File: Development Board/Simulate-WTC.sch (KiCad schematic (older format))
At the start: 5 parts

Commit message: main sheets created
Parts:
- J? (x2): symbol conn:GS3 -> QPACE-DevelopmentBoard-rescue:GS3-conn
- R? (x2): symbol device:R -> QPACE-DevelopmentBoard-rescue:R-device
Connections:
- net labels added: CCDR_UART_RX, CCDR_UART_TX, I2C_SCK, NRST, RF_UART_RX, RF_UART_TX, SWCLK, SWDIO, SWO
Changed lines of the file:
@@
 EESchema Schematic File Version 4
 LIBS:QPACE-DevelopmentBoard-cache
-LIBS:WTC-cache
 EELAYER 26 0
 EELAYER END
 $Descr A4 11693 8268
 encoding utf-8
-Sheet 3 3
+Sheet 3 9
 Title ""
 Date ""
@@
 BOOT0
 $Comp
-L device:R R?
+L QPACE-DevelopmentBoard-rescue:R-device R?
 U 1 1 5C997057
 P 1700 2800
+AR Path="/5C997057" Ref="R?"  Part="1"
+AR Path="/5C7F8729/5C997057" Ref="R?"  Part="1"
 F 0 "R?" V 1907 2800 50  0000 C CNN
 F 1 "100k" V 1816 2800 50  0000 C CNN
@@
 $EndComp
 $Comp
-L conn:GS3 J?
+L QPACE-DevelopmentBoard-rescue:GS3-conn J?
 U 1 1 5C9970FC
 P 1400 2800
+AR Path="/5C9970FC" Ref="J?"  Part="1"
+AR Path="/5C7F8729/5C9970FC" Ref="J?"  Part="1"
 F 0 "J?" H 1400 3105 50  0000 C CNN
 F 1 "GS3" H 1400 3014 50  0000 C CNN
@@
 $EndComp
 $Comp
-L device:R R?
+L QPACE-DevelopmentBoard-rescue:R-device R?
 U 1 1 5C9971B9
 P 1700 3300
+AR Path="/5C9971B9" Ref="R?"  Part="1"
+AR Path="/5C7F8729/5C9971B9" Ref="R?"  Part="1"
 F 0 "R?" V 1907 3300 50  0000 C CNN
 F 1 "100k" V 1816 3300 50  0000 C CNN
@@
 $EndComp
 $Comp
-L conn:GS3 J?
+L QPACE-DevelopmentBoard-rescue:GS3-conn J?
 U 1 1 5C9971DB
 P 1400 3300
+AR Path="/5C9971DB" Ref="J?"  Part="1"
+AR Path="/5C7F8729/5C9971DB" Ref="J?"  Part="1"
 F 0 "J?" H 1400 3605 50  0000 C CNN
 F 1 "GS3" H 1400 3514 50  0000 C CNN
@@
 NoConn ~ 3100 4500
 NoConn ~ 3100 4400
+Text HLabel 9000 1700 2    50   Input ~ 0
+SWCLK
+Text HLabel 9000 1800 2    50   Input ~ 0
+SWDIO
+Text HLabel 9000 1900 2    50   Input ~ 0
+NRST
+Text HLabel 9000 2000 2    50   Input ~ 0
+SWO
+Text HLabel 9000 2150 2    50   Input ~ 0
+RF_UART_TX
+Text HLabel 9000 2250 2    50   Input ~ 0
+RF_UART_RX
+Text HLabel 9000 2350 2    50   Input ~ 0
+CCDR_UART_RX
+Text HLabel 9000 2450 2    50   Input ~ 0
+CCDR_UART_TX
+Text HLabel 9000 2800 2    50   Input ~ 0
+I2C_SDA
+Text HLabel 9000 2900 2    50   Input ~ 0
+I2C_SCK
 $EndSCHEMATC

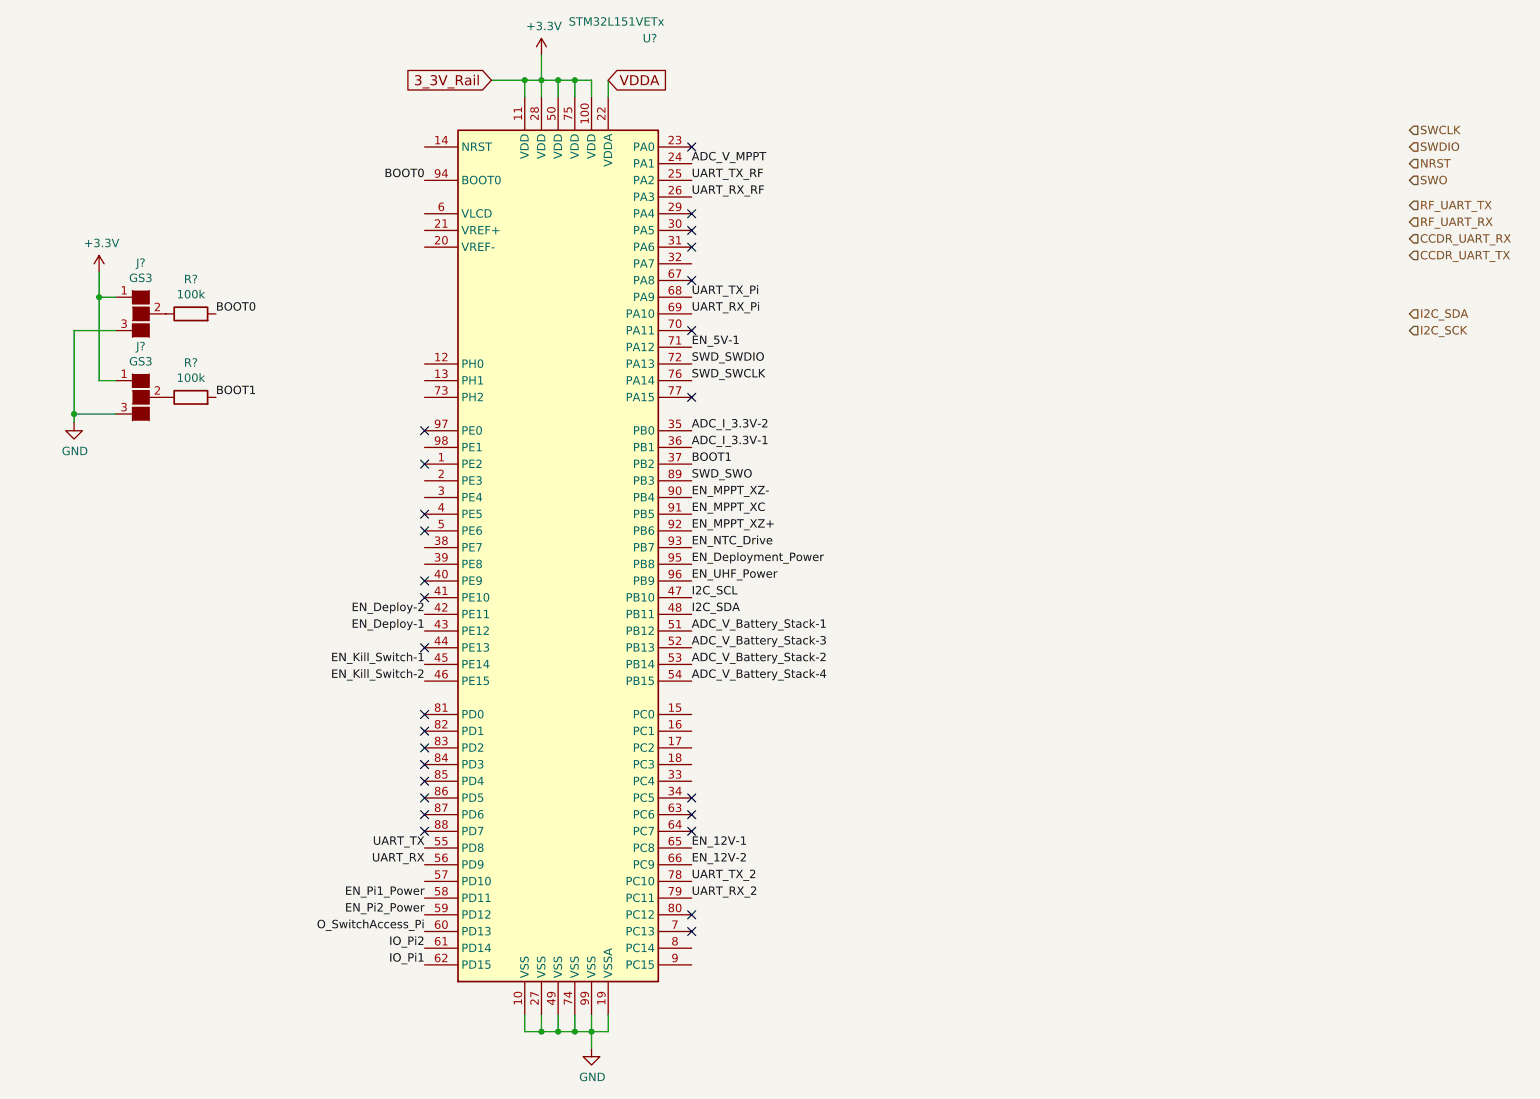
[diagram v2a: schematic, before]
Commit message: added KISS description, UART-I2C chip
keep it simple, stupid. Goal is to create software development board for sub-system comms
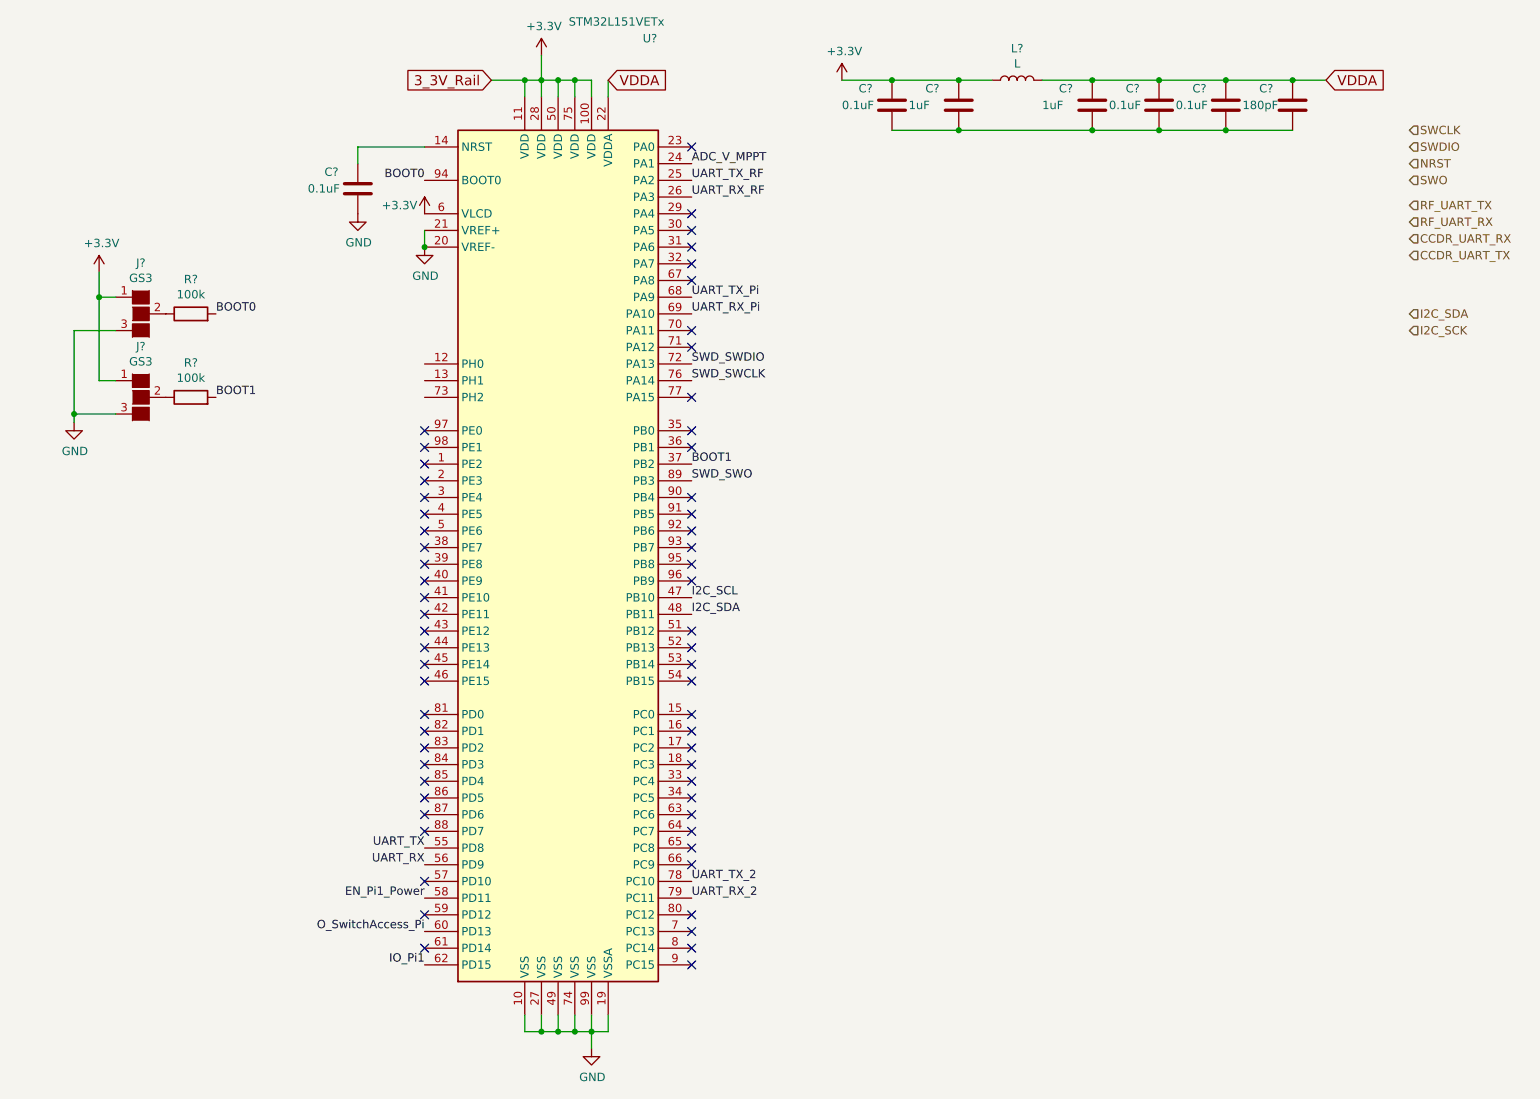
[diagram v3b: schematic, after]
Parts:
- added C? (x4): 0.1uF, symbol device:C
- added C? (x2): 1uF, symbol device:C
- added C?: 180pF, symbol device:C
- added L?: L, symbol device:L
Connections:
- net +3V3: now also U?.6 (VLCD), C?.1, C?.1, L?.1
- net GND: now also U?.20 (VREF-), U?.21 (VREF+), C?.2
- net VDDA: now also C?.1, C?.1, C?.1, C?.1, L?.2
- net at U?.14 (NRST): now also C?.1
- net ADC_I_3.3V-1: no longer names the net of U?.36 (PB1)
- net ADC_I_3.3V-2: no longer names the net of U?.35 (PB0)
- net ADC_V_Battery_Stack-1: no longer names the net of U?.51 (PB12)
- net ADC_V_Battery_Stack-2: no longer names the net of U?.53 (PB14)
- net ADC_V_Battery_Stack-3: no longer names the net of U?.52 (PB13)
- net ADC_V_Battery_Stack-4: no longer names the net of U?.54 (PB15)
- net EN_12V-1: no longer names the net of U?.65 (PC8)
- net EN_12V-2: no longer names the net of U?.66 (PC9)
- net EN_5V-1: no longer names the net of U?.71 (PA12)
- net EN_Deploy-1: no longer names the net of U?.43 (PE12)
- net EN_Deploy-2: no longer names the net of U?.42 (PE11)
- net EN_Deployment_Power: no longer names the net of U?.95 (PB8)
- net EN_Kill_Switch-1: no longer names the net of U?.45 (PE14)
- net EN_Kill_Switch-2: no longer names the net of U?.46 (PE15)
- net EN_MPPT_XC: no longer names the net of U?.91 (PB5)
- net EN_MPPT_XZ+: no longer names the net of U?.92 (PB6)
- net EN_MPPT_XZ-: no longer names the net of U?.90 (PB4)
- net EN_NTC_Drive: no longer names the net of U?.93 (PB7)
- net EN_Pi2_Power: no longer names the net of U?.59 (PD12)
- net EN_UHF_Power: no longer names the net of U?.96 (PB9)
- net IO_Pi2: no longer names the net of U?.61 (PD14)
- new net: C?.2, C?.2, C?.2, C?.2, C?.2, C?.2
- no-connect marks 27 -> 62

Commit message: reduced complexity
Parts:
- added J?: Avionics Stack Connector, symbol conn:Conn_02x20_Odd_Even
- added J?: STM32_UARTport, symbol conn:Conn_01x03
- added R? (x2): 51, symbol device:R
- added R? (x2): 10k, symbol device:R
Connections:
- net I2C_SCL is gone; now on net I2C_SCK: U?.47 (PB10)
- net I2C_SDA is gone; now on net I2C_SCK: U?.48 (PB11)
- net SWD_SWO is gone; now on net SWO: U?.89 (PB3)
- net UART_RX_2 is gone; now on net RF_UART_RX: U?.79 (PC11)
- net UART_RX_Pi is gone; now on net CCDR_UART_RX: U?.69 (PA10)
- net UART_TX_2 is gone; now on net RF_UART_TX: U?.78 (PC10)
- net UART_TX_Pi is gone; now on net CCDR_UART_TX: U?.68 (PA9)
- net +3V3: now also R?.1, R?.1
- net GND: now also J?.21 (Pin_21), J?.22 (Pin_22), J?.23 (Pin_23), J?.24 (Pin_24), J?.25 (Pin_25), J?.26 (Pin_26), J?.3 (Pin_3)
- net I2C_SCK: now also J?.11 (Pin_11), J?.13 (Pin_13)
- net NRST: now also C?.1, U?.14 (NRST)
- net SWCLK: now also R?.1, R?.2
- net SWDIO: now also R?.1, R?.2
- net SWD_SWCLK: now also R?.2
- net SWD_SWDIO: now also R?.2
- net UART_RX_RF: now also J?.2 (Pin_2)
- net UART_TX_RF: now also J?.1 (Pin_1)
- net EN_Pi2_Power: now reaches U?.59 (PD12)
- net IO_Pi2: now reaches U?.61 (PD14)
- net EN_12V-1: now reaches U?.65 (PC8)
- net EN_12V-1: now also J?.17 (Pin_17)
- net EN_12V-2: now reaches U?.66 (PC9)
- net EN_12V-2: now also J?.18 (Pin_18)
- net EN_5V-1: now reaches U?.71 (PA12)
- net EN_5V-1: now also U?.81 (PD0), J?.29 (Pin_29)
- net EN_5V-2: now reaches U?.73 (PH2)
- net EN_5V-2: now also J?.30 (Pin_30)
- new net 12V_Rail: J?.15 (Pin_15)
- new net 3V3_Rail: J?.38 (Pin_38), J?.40 (Pin_40)
- new net 5V_Rail: J?.35 (Pin_35), J?.37 (Pin_37), J?.39 (Pin_39)
- new net EN_Pi1_Pwr: J?.6 (Pin_6)
- new net EN_Pi2_Pwr: J?.8 (Pin_8)
- new net EN_Pi_Mux: J?.2 (Pin_2)
- new net Pi1_GPIO: J?.9 (Pin_9)
- new net Pi2_GPIO: J?.4 (Pin_4)
- new net UART_RX_Pi1: J?.7 (Pin_7)
- new net UART_RX_Pi2: J?.3 (Pin_3)
- new net UART_TX_Pi1: J?.5 (Pin_5)
- new net UART_TX_Pi2: J?.1 (Pin_1)
- new net Vbat: J?.31 (Pin_31), J?.32 (Pin_32), J?.33 (Pin_33), J?.34 (Pin_34)
- no-connect marks 62 -> 65
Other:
- note added: "Use the "Avionics Stack Connector" to attach \nto the engineering model to test functionality"

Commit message: Q-PACE Devboard V0
This should complete the KiCad Schematic and PCB files. Parts should be in FSI inventory.
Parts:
- removed J? (x2): GS3, Connectors:GS3, symbol QPACE-DevelopmentBoard-rescue:GS3-conn
- removed J?: Avionics Stack Connector, symbol conn:Conn_02x20_Odd_Even
- removed J?: STM32_UARTport, symbol conn:Conn_01x03
- C10, C11, C6, C7, C8, C9: renamed from C?; footprint (none) -> Capacitors_SMD:C_0805; symbol device:C -> QPACE-DevelopmentBoard-rescue:C-device
- C12: renamed from C?; footprint (none) -> Capacitors_SMD:C_0603; symbol device:C -> QPACE-DevelopmentBoard-rescue:C-device
- L1: renamed from L?; footprint (none) -> Inductors_SMD:L_0603; symbol device:L -> QPACE-DevelopmentBoard-rescue:L-device
- R10, R9: renamed from R?; footprint (none) -> Resistors_SMD:R_0805
- R11, R12, R13, R14: renamed from R?; footprint (none) -> Resistors_SMD:R_0805; symbol device:R -> QPACE-DevelopmentBoard-rescue:R-device
- U3: renamed from U?; footprint Package_QFP:LQFP-100_14x14mm_P0.5mm -> Housings_QFP:LQFP-100_14x14mm_Pitch0.5mm
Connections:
- net O_SwitchAccess_Pi is gone; now on net EN_Pi_Mux: U3.60 (PD13)
- net EN_5V-1: no longer U3.81 (PD0)
- net GND: now also C10.2, C11.2, C12.2, C7.2, C8.2, C9.2, R10.1, R9.1
- net I2C_SCK: no longer U3.47 (PB10)
- net EN_Pi1_Power renamed EN_PiPwr
- net EN_Pi2_Power: no longer names the net of U3.59 (PD12)
- net UART_RX_RF renamed extra_RX
- net UART_TX_RF renamed extra_TX
- new net I2C_SDA: U3.47 (PB10)
- no-connect marks 65 -> 58

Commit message: ready for production
passed all KiCad error checking. schematic and pcblayout were both validated. ready to be ordered
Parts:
- R13, R14: value 10k -> 4.99K
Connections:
- net I2C_SCK is gone; now on net I2C_SDA: U3.48 (PB11)
- net +3V3: now also U3.21 (VREF+)
- net GND: no longer U3.21 (VREF+)
- net I2C_SDA: no longer U3.47 (PB10)
- net ADC_V_MPPT: no longer names the net of U3.24 (PA1)
- net EN_12V-1: no longer names the net of U3.65 (PC8)
- net EN_12V-2: no longer names the net of U3.66 (PC9)
- net EN_5V-1: no longer names the net of U3.71 (PA12)
- net EN_5V-2: no longer names the net of U3.73 (PH2)
- net EN_Pi_Mux: no longer names the net of U3.60 (PD13)
- net IO_Pi1 renamed PiHeartBeat
- net IO_Pi2: no longer names the net of U3.61 (PD14)
- net UART_RX: no longer names the net of U3.56 (PD9)
- net UART_TX: no longer names the net of U3.55 (PD8)
- new net I2C_SCL: U3.47 (PB10)
- no-connect marks 58 -> 69
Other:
- moved on the sheet: C10, C11, C12, C7, C8, C9, L1
